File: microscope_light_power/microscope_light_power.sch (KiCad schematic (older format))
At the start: 15 parts

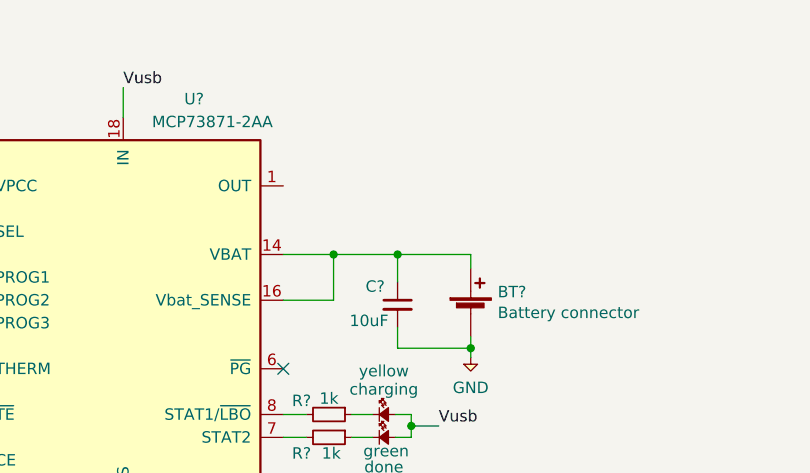
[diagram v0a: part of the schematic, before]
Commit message: Add some bypass capacitance to the battery management unit power output.
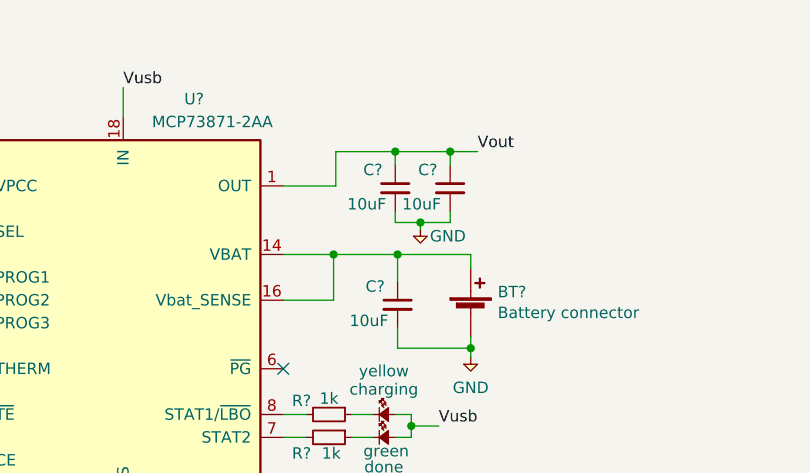
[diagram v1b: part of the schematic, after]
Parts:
- added C? (x2): 10uF, Capacitors_SMD:C_0805_HandSoldering, symbol C_Small
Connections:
- net GND: now also C?.2, C?.2
- net Vout: now reaches U?.1 (OUT), U?.20 (OUT)
- net Vout: now also C?.1, C?.1
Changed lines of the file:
@@
 	2450 2040 2310 2040
 Connection ~ 2310 2040
+Text Label 5110 1090 0    50   ~ 0
+Vout
+Wire Wire Line
+	4260 1240 4490 1240
+$Comp
+L C_Small C?
+U 1 1 59DC8009
+P 4750 1250
+F 0 "C?" H 4610 1330 50  0000 L CNN
+F 1 "10uF" H 4540 1180 50  0000 L CNN
+F 2 "Capacitors_SMD:C_0805_HandSoldering" H 4750 1250 50  0001 C CNN
+F 3 "" H 4750 1250 50  0001 C CNN
+	1    4750 1250
+	1    0    0    -1
+$EndComp
+$Comp
+L C_Small C?
+U 1 1 59DC8053
+P 4990 1250
+F 0 "C?" H 4850 1330 50  0000 L CNN
+F 1 "10uF" H 4780 1180 50  0000 L CNN
+F 2 "Capacitors_SMD:C_0805_HandSoldering" H 4990 1250 50  0001 C CNN
+F 3 "" H 4990 1250 50  0001 C CNN
+	1    4990 1250
+	1    0    0    -1
+$EndComp
+Wire Wire Line
+	4990 1090 4990 1150
+Wire Wire Line
+	4490 1090 5110 1090
+Wire Wire Line
+	4750 1090 4750 1150
+Wire Wire Line
+	4490 1240 4490 1090
+Connection ~ 4750 1090
+Connection ~ 4990 1090
+Wire Wire Line
+	4750 1350 4750 1400
+Wire Wire Line
+	4750 1400 4990 1400
+Wire Wire Line
+	4990 1400 4990 1350
+$Comp
+L GND #PWR?
+U 1 1 59DCA58C
+P 4860 1430
+F 0 "#PWR?" H 4730 1470 50  0001 L CNN
+F 1 "GND" H 4980 1400 50  0000 C CNN
+F 2 "" H 4860 1430 50  0001 C CNN
+F 3 "" H 4860 1430 50  0001 C CNN
+	1    4860 1430
+	1    0    0    -1
+$EndComp
+Wire Wire Line
+	4860 1430 4860 1400
+Connection ~ 4860 1400
 $EndSCHEMATC

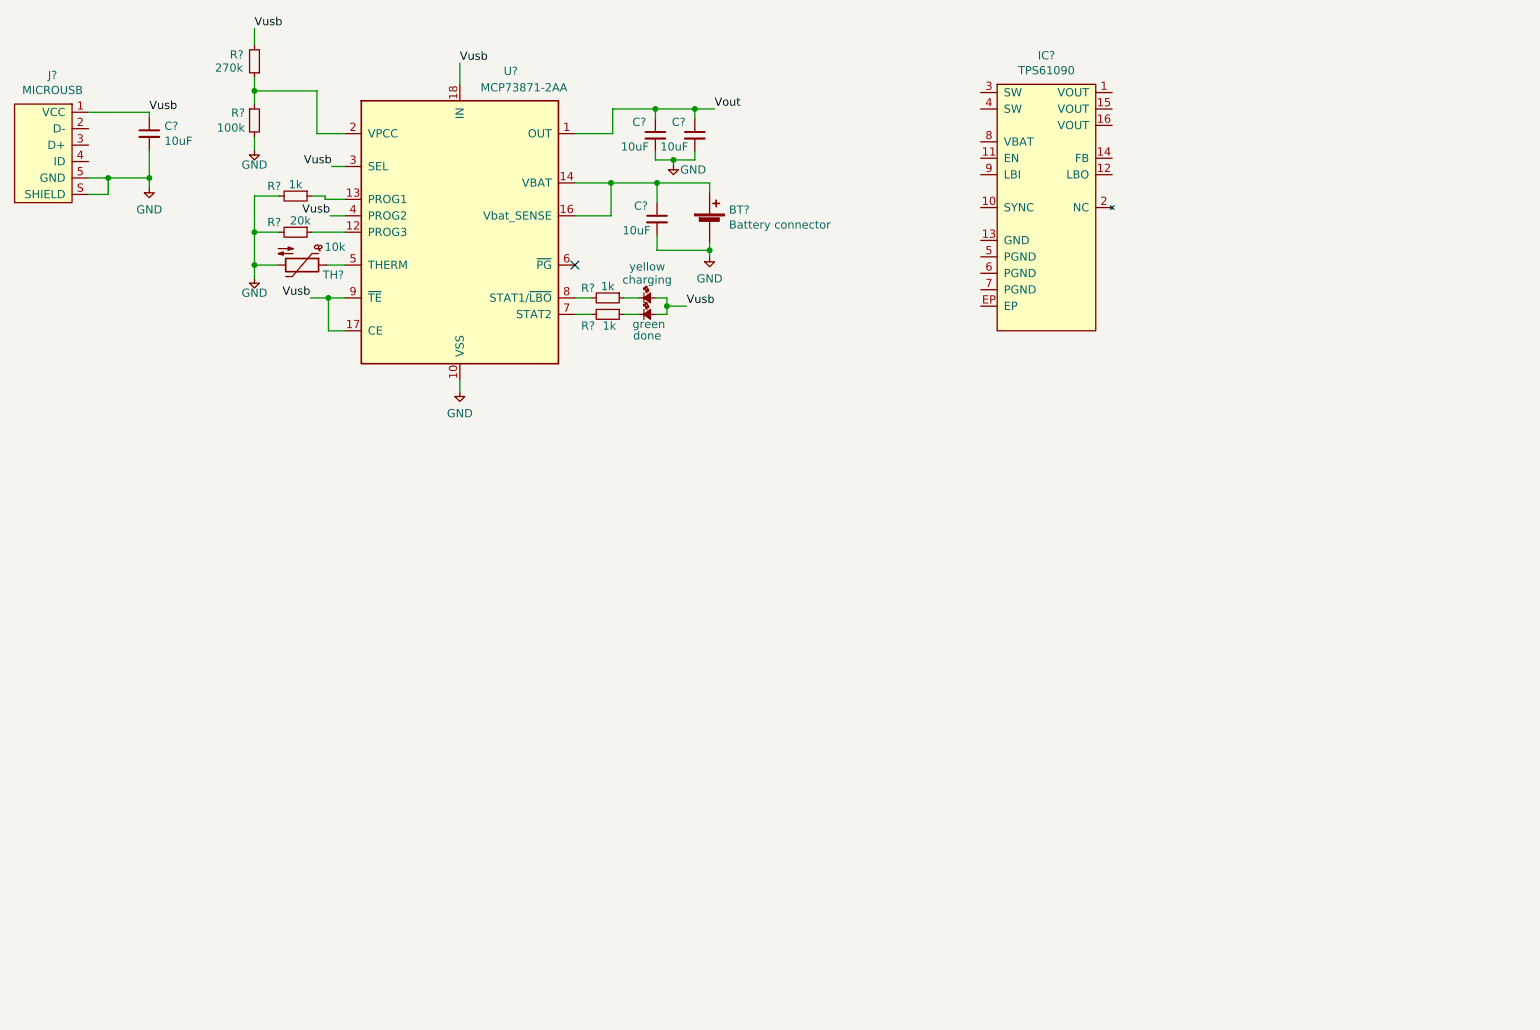
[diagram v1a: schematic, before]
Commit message: Drew schematic for the boost converter. Last bit is connectors and small detail work.
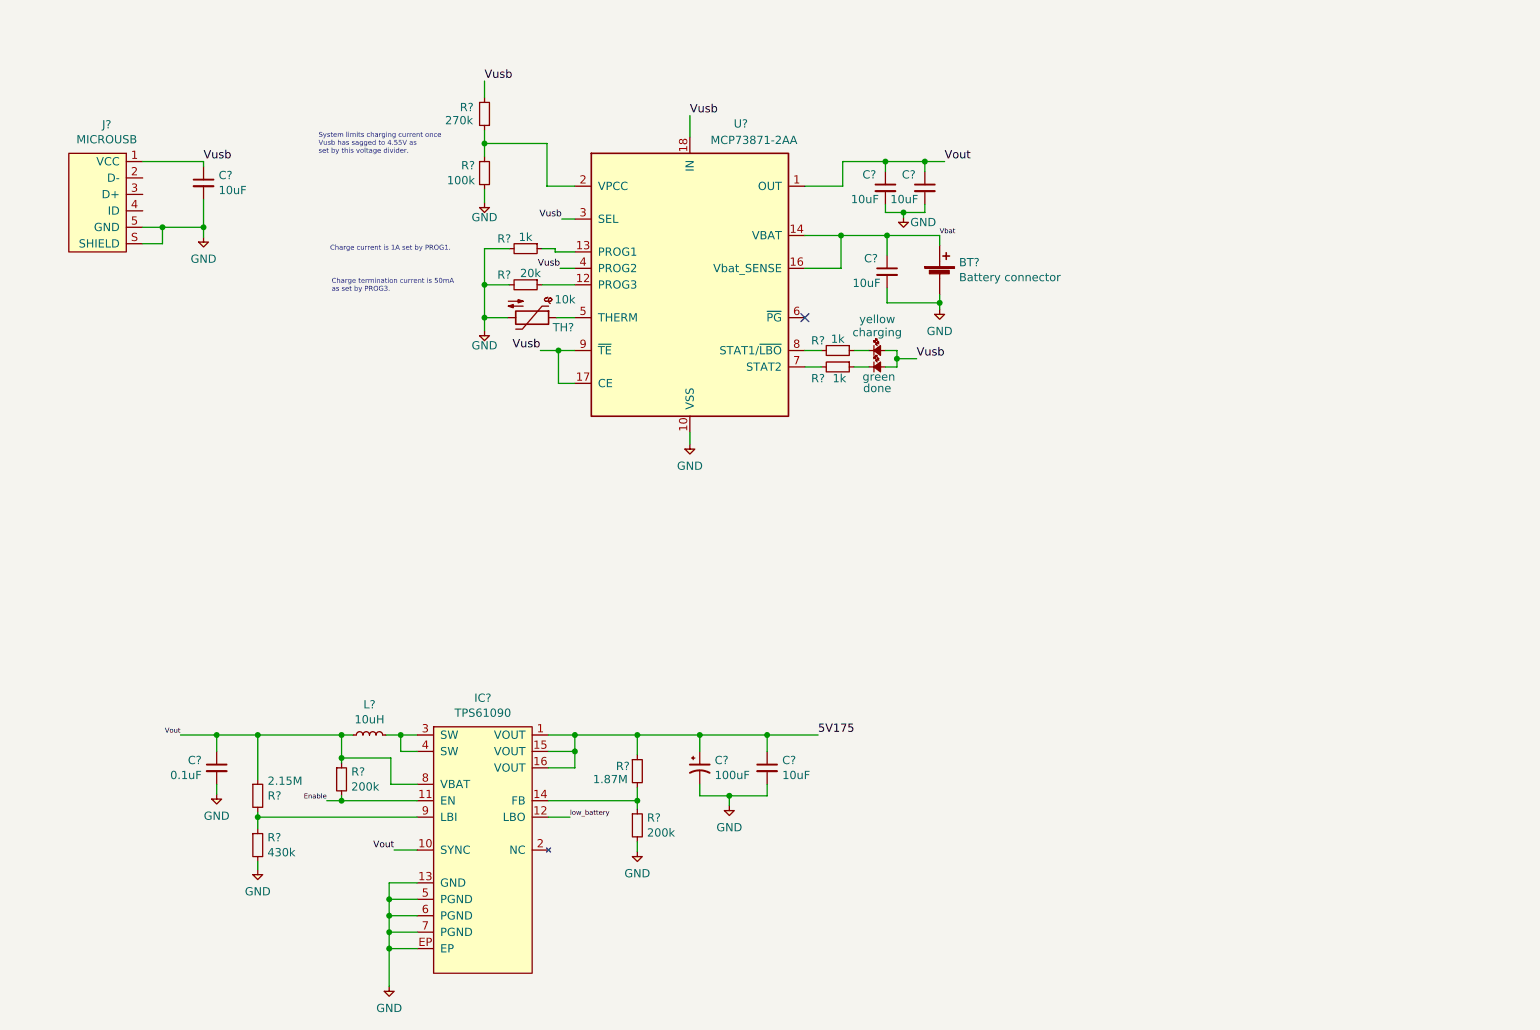
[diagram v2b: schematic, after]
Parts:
- added C?: 0.1uF, Capacitors_SMD:C_0603_HandSoldering, symbol C_Small
- added C?: 100uF, Capacitors_ThroughHole:CP_Radial_D8.0mm_P3.50mm, symbol CP1_Small
- added C?: 10uF, Capacitors_SMD:C_0805_HandSoldering, symbol C_Small
- added L?: 10uH, symbol L_Small
- added R?: 430k, Resistors_SMD:R_0603_HandSoldering, symbol R_Small
- added R?: 2.15M, Resistors_SMD:R_0603_HandSoldering, symbol R_Small
- added R? (x2): 200k, Resistors_SMD:R_0603_HandSoldering, symbol R_Small
- added R?: 1.87M, Resistors_SMD:R_0603_HandSoldering, symbol R_Small
- TH?: footprint (none) -> Resistors_Universal:Resistor_SMD+THTuniversal_0805to1206_RM10_HandSoldering
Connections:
- net GND: now also IC?.13 (GND), IC?.5 (PGND), IC?.6 (PGND), IC?.7 (PGND), IC?.EP, C?.2, C?.2, C?.2, R?.2, R?.2
- net Vout: now also IC?.10 (SYNC), IC?.8 (VBAT), C?.1, L?.1, R?.1, R?.1
- net 5V175: now reaches IC?.1 (VOUT)
- net 5V175: now also IC?.15 (VOUT), IC?.16 (VOUT), C?.1, C?.1, R?.1
- net Enable: now reaches IC?.11 (EN)
- net Enable: now also R?.2
- net low_battery: now reaches IC?.12 (LBO)
- net at IC?.14 (FB): now also R?.1, R?.2
- net at IC?.3 (SW): now also IC?.4 (SW), L?.2
- net at IC?.9 (LBI): now also R?.1, R?.2
- net Vbat: now reaches BT?.1 (+), C?.1, U?.14 (VBAT), U?.15 (VBAT), U?.16 (Vbat_SENSE)
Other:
- note added: "Charge current is 1A set by PROG1."
- note added: "Charge termination current is 50mA \nas set by PROG3."
- note added: "System limits charging current once \nVusb has sagged to 4.55V as \nset by this voltage divider."
- moved on the sheet: BT?, C?, IC?, J?, R?, TH?, U?, green, yellow

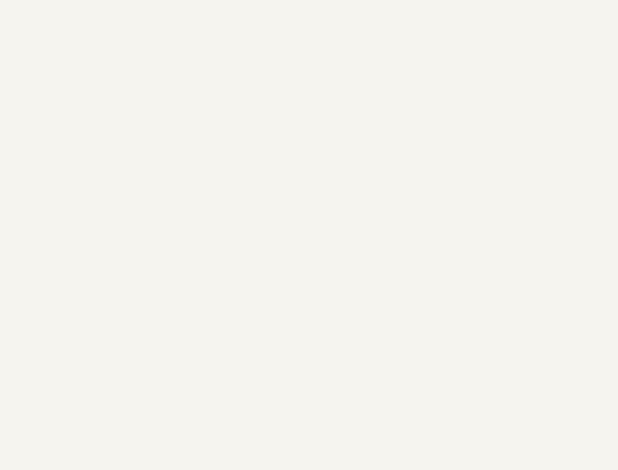
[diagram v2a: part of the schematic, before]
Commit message: Added M3 mounting holes in schematic.
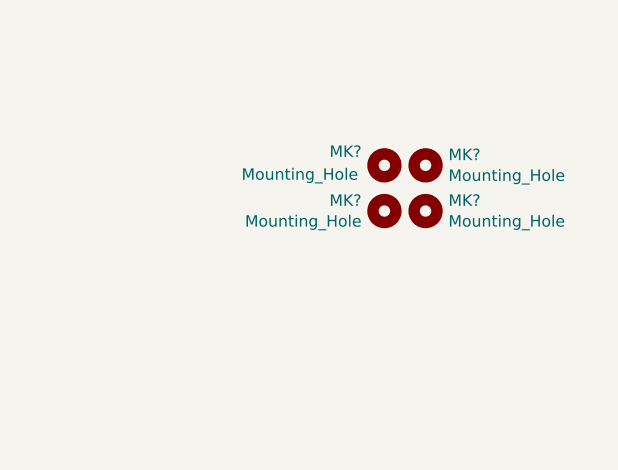
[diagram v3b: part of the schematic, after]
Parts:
- added MK? (x4): Mounting_Hole, Mounting_Holes:MountingHole_3.2mm_M3_ISO14580, symbol Mounting_Hole
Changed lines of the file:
@@
 	3300 6200 3130 6200
 Connection ~ 3130 6200
+$Comp
+L Mounting_Hole MK?
+U 1 1 59FAECB9
+P 9290 1470
+F 0 "MK?" H 9390 1516 50  0000 L CNN
+F 1 "Mounting_Hole" H 9390 1425 50  0000 L CNN
+F 2 "Mounting_Holes:MountingHole_3.2mm_M3_ISO14580" H 9290 1470 50  0001 C CNN
+F 3 "" H 9290 1470 50  0001 C CNN
+	1    9290 1470
+	1    0    0    -1
+$EndComp
+$Comp
+L Mounting_Hole MK?
+U 1 1 59FAF2DD
+P 9290 1670
+F 0 "MK?" H 9390 1716 50  0000 L CNN
+F 1 "Mounting_Hole" H 9390 1625 50  0000 L CNN
+F 2 "Mounting_Holes:MountingHole_3.2mm_M3_ISO14580" H 9290 1670 50  0001 C CNN
+F 3 "" H 9290 1670 50  0001 C CNN
+	1    9290 1670
+	1    0    0    -1
+$EndComp
+$Comp
+L Mounting_Hole MK?
+U 1 1 59FAF43B
+P 9110 1670
+F 0 "MK?" H 9010 1716 50  0000 R CNN
+F 1 "Mounting_Hole" H 9010 1625 50  0000 R CNN
+F 2 "Mounting_Holes:MountingHole_3.2mm_M3_ISO14580" H 9110 1670 50  0001 C CNN
+F 3 "" H 9110 1670 50  0001 C CNN
+	1    9110 1670
+	1    0    0    -1
+$EndComp
+$Comp
+L Mounting_Hole MK?
+U 1 1 59FAF70C
+P 9110 1470
+F 0 "MK?" V 9050 1300 50  0000 C CNN
+F 1 "Mounting_Hole" V 9150 1100 50  0000 C CNN
+F 2 "Mounting_Holes:MountingHole_3.2mm_M3_ISO14580" H 9110 1470 50  0001 C CNN
+F 3 "" H 9110 1470 50  0001 C CNN
+	1    9110 1470
+	0    1    1    0
+$EndComp
 $EndSCHEMATC
